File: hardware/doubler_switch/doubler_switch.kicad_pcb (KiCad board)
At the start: 2 copper layers, 54 parts, among them J101 CONN_01X06, U101 CONN_SMA_2GND, U102 PE42521, U103 74HC04_FULL, U104 AMMP-6120, U105 PE42521, U106 PE42521, U107 MASW-008322-TR1000, U108 PE42521, U109 CONN_SMA_2GND, U110 CONN_SMA_2GND, U111 TPS255xx, U112 LTC1983

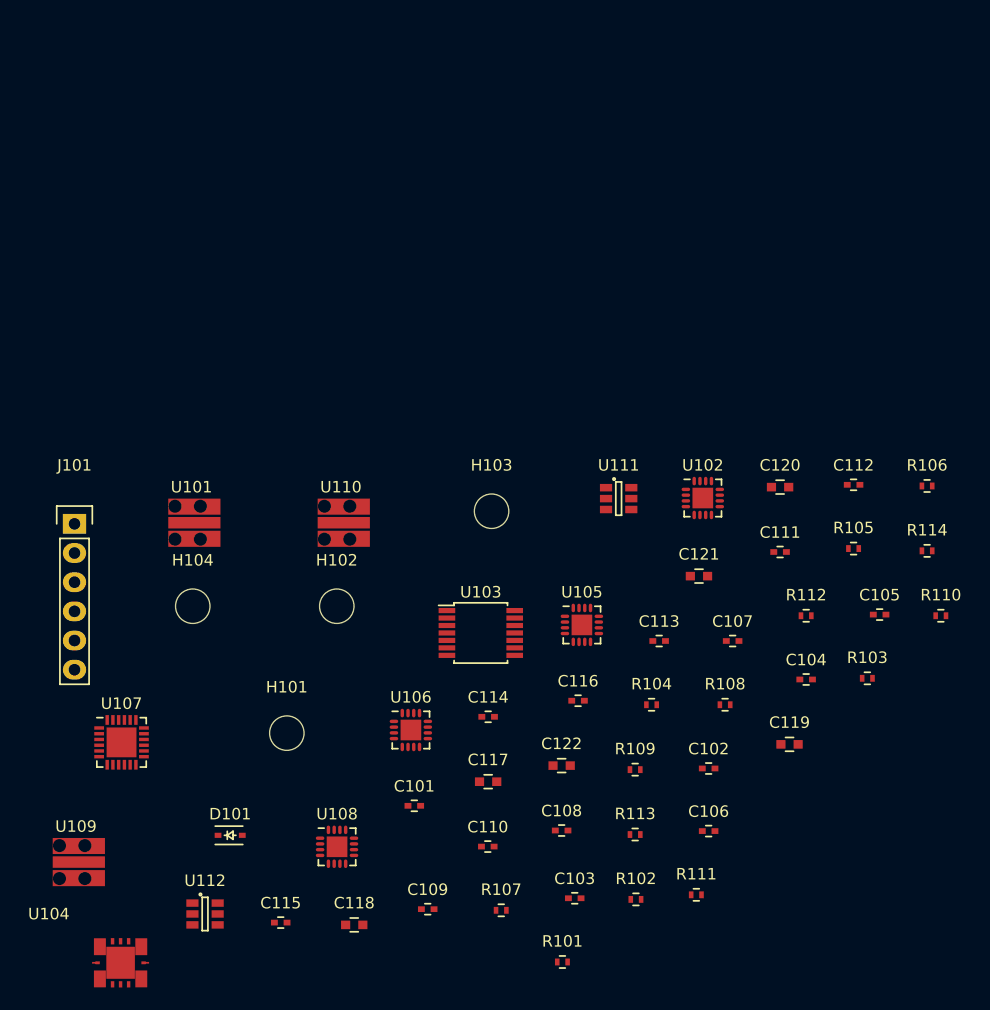
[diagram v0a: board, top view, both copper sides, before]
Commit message: finished vna port switch/multiplier board
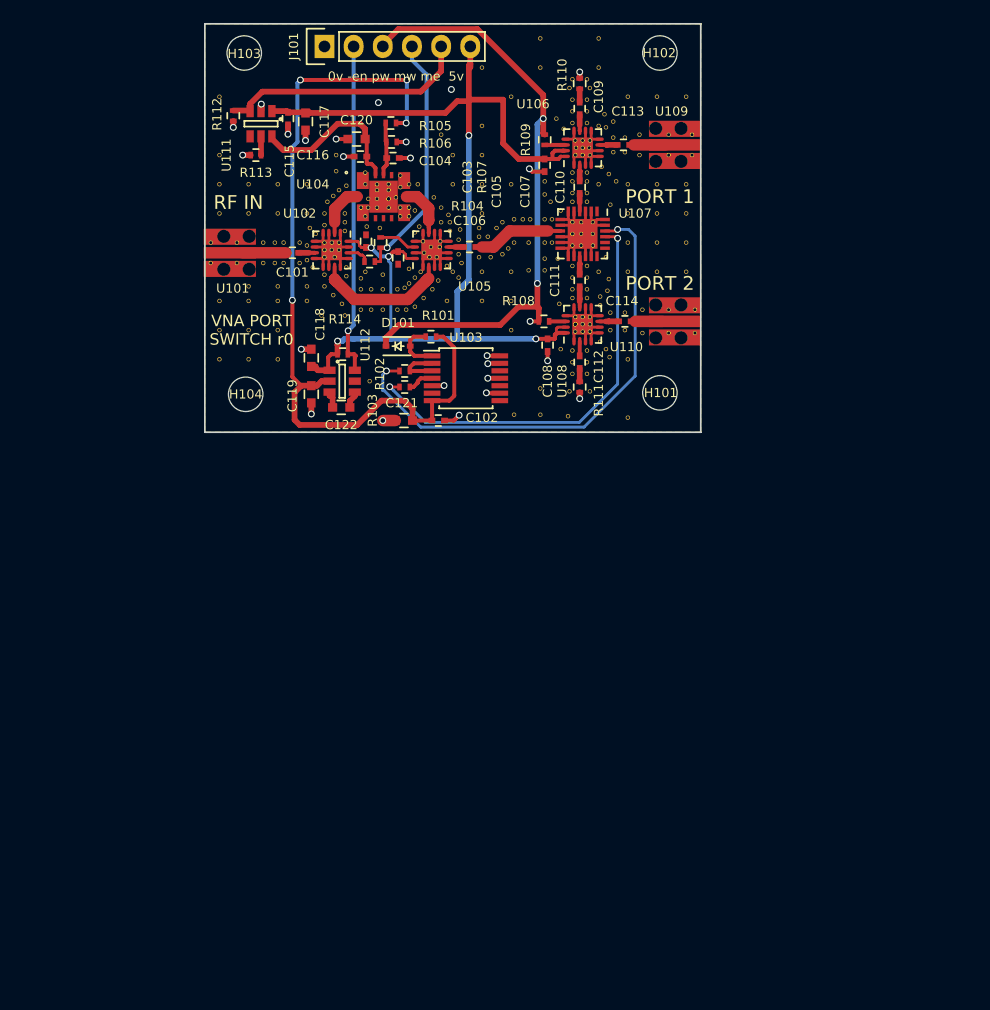
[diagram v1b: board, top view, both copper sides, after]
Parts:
- added REF**: VIA_OSH4LAYER_MIN, vna_footprints:VIA_OSH4LAYER_MIN, F.Cu at (229.7, 45.7)
- added REF**: VIA_OSH4LAYER_MIN, vna_footprints:VIA_OSH4LAYER_MIN, F.Cu at (218.2, 51.6)
- added REF**: VIA_OSH4LAYER_MIN, vna_footprints:VIA_OSH4LAYER_MIN, F.Cu at (238.8, 40.6)
- added REF**: VIA_OSH4LAYER_MIN, vna_footprints:VIA_OSH4LAYER_MIN, F.Cu at (238.8, 50.8)
- added REF**: VIA_OSH4LAYER_MIN, vna_footprints:VIA_OSH4LAYER_MIN, F.Cu at (233.7, 50.8)
- added REF**: VIA_OSH4LAYER_MIN, vna_footprints:VIA_OSH4LAYER_MIN, F.Cu at (238.8, 55.9)
- added REF**: VIA_OSH4LAYER_MIN, vna_footprints:VIA_OSH4LAYER_MIN, F.Cu at (238.8, 48.3)
- added REF**: VIA_OSH4LAYER_MIN, vna_footprints:VIA_OSH4LAYER_MIN, F.Cu at (238.8, 53.3)
- added REF**: VIA_OSH4LAYER_MIN, vna_footprints:VIA_OSH4LAYER_MIN, F.Cu at (233.7, 53.3)
- added REF**: VIA_OSH4LAYER_MIN, vna_footprints:VIA_OSH4LAYER_MIN, F.Cu at (236.2, 53.3)
- added REF**: VIA_OSH4LAYER_MIN, vna_footprints:VIA_OSH4LAYER_MIN, F.Cu at (223.5, 61.0)
- added REF**: VIA_OSH4LAYER_MIN, vna_footprints:VIA_OSH4LAYER_MIN, F.Cu at (226.4, 55.8)
- added REF**: VIA_OSH4LAYER_MIN, vna_footprints:VIA_OSH4LAYER_MIN, F.Cu at (218.9, 56.4)
- added REF**: VIA_OSH4LAYER_MIN, vna_footprints:VIA_OSH4LAYER_MIN, F.Cu at (231.1, 55.9)
- added REF**: VIA_OSH4LAYER_MIN, vna_footprints:VIA_OSH4LAYER_MIN, F.Cu at (233.7, 55.9)
- added REF**: VIA_OSH4LAYER_MIN, vna_footprints:VIA_OSH4LAYER_MIN, F.Cu at (236.2, 55.9)
- added REF**: VIA_OSH4LAYER_MIN, vna_footprints:VIA_OSH4LAYER_MIN, F.Cu at (236.2, 50.8)
- added REF**: VIA_OSH4LAYER_MIN, vna_footprints:VIA_OSH4LAYER_MIN, F.Cu at (236.2, 48.3)
- added REF**: VIA_OSH4LAYER_MIN, vna_footprints:VIA_OSH4LAYER_MIN, F.Cu at (233.7, 48.3)
- added REF**: VIA_OSH4LAYER_MIN, vna_footprints:VIA_OSH4LAYER_MIN, F.Cu at (231.1, 48.3)
- added REF**: VIA_OSH4LAYER_MIN, vna_footprints:VIA_OSH4LAYER_MIN, F.Cu at (231.1, 43.2)
- added REF**: VIA_OSH4LAYER_MIN, vna_footprints:VIA_OSH4LAYER_MIN, F.Cu at (221.0, 43.2)
- added REF**: VIA_OSH4LAYER_MIN, vna_footprints:VIA_OSH4LAYER_MIN, F.Cu at (221.0, 45.7)
- added REF**: VIA_OSH4LAYER_MIN, vna_footprints:VIA_OSH4LAYER_MIN, F.Cu at (217.9, 55.4)
- added REF**: VIA_OSH4LAYER_MIN, vna_footprints:VIA_OSH4LAYER_MIN, F.Cu at (226.4, 48.0)
- added REF**: VIA_OSH4LAYER_MIN, vna_footprints:VIA_OSH4LAYER_MIN, F.Cu at (223.5, 48.3)
- added REF**: VIA_OSH4LAYER_MIN, vna_footprints:VIA_OSH4LAYER_MIN, F.Cu at (221.0, 50.8)
- added REF**: VIA_OSH4LAYER_MIN, vna_footprints:VIA_OSH4LAYER_MIN, F.Cu at (221.0, 58.4)
- added REF**: VIA_OSH4LAYER_MIN, vna_footprints:VIA_OSH4LAYER_MIN, F.Cu at (217.9, 58.4)
- added REF**: VIA_OSH4LAYER_MIN, vna_footprints:VIA_OSH4LAYER_MIN, F.Cu at (223.5, 55.9)
- added REF**: VIA_OSH4LAYER_MIN, vna_footprints:VIA_OSH4LAYER_MIN, F.Cu at (221.0, 55.9)
- added REF**: VIA_OSH4LAYER_MIN, vna_footprints:VIA_OSH4LAYER_MIN, F.Cu at (218.4, 55.9)
- added REF**: VIA_OSH4LAYER_MIN, vna_footprints:VIA_OSH4LAYER_MIN, F.Cu at (218.4, 48.3)
- added REF**: VIA_OSH4LAYER_MIN, vna_footprints:VIA_OSH4LAYER_MIN, F.Cu at (208.3, 45.7)
- added REF**: VIA_OSH4LAYER_MIN, vna_footprints:VIA_OSH4LAYER_MIN, F.Cu at (227.7, 58.7)
- added REF**: VIA_OSH4LAYER_MIN, vna_footprints:VIA_OSH4LAYER_MIN, F.Cu at (205.7, 48.3)
- added REF**: VIA_OSH4LAYER_MIN, vna_footprints:VIA_OSH4LAYER_MIN, F.Cu at (203.2, 48.3)
- added REF**: VIA_OSH4LAYER_MIN, vna_footprints:VIA_OSH4LAYER_MIN, F.Cu at (200.7, 48.3)
- added REF**: VIA_OSH4LAYER_MIN, vna_footprints:VIA_OSH4LAYER_MIN, F.Cu at (198.1, 48.3)
- added REF**: VIA_OSH4LAYER_MIN, vna_footprints:VIA_OSH4LAYER_MIN, F.Cu at (198.1, 50.8)
- added REF**: VIA_OSH4LAYER_MIN, vna_footprints:VIA_OSH4LAYER_MIN, F.Cu at (200.7, 50.8)
- added REF**: VIA_OSH4LAYER_MIN, vna_footprints:VIA_OSH4LAYER_MIN, F.Cu at (203.2, 50.8)
- added REF**: VIA_OSH4LAYER_MIN, vna_footprints:VIA_OSH4LAYER_MIN, F.Cu at (203.2, 63.5)
- added REF**: VIA_OSH4LAYER_MIN, vna_footprints:VIA_OSH4LAYER_MIN, F.Cu at (198.1, 63.5)
- added REF**: VIA_OSH4LAYER_MIN, vna_footprints:VIA_OSH4LAYER_MIN, F.Cu at (198.1, 61.0)
- added REF**: VIA_OSH4LAYER_MIN, vna_footprints:VIA_OSH4LAYER_MIN, F.Cu at (227.8, 62.6)
- added REF**: VIA_OSH4LAYER_MIN, vna_footprints:VIA_OSH4LAYER_MIN, F.Cu at (203.2, 61.0)
- added REF**: VIA_OSH4LAYER_MIN, vna_footprints:VIA_OSH4LAYER_MIN, F.Cu at (200.7, 61.0)
- added REF**: VIA_OSH4LAYER_MIN, vna_footprints:VIA_OSH4LAYER_MIN, F.Cu at (200.7, 57.1)
- added REF**: VIA_OSH4LAYER_MIN, vna_footprints:VIA_OSH4LAYER_MIN, F.Cu at (203.2, 57.1)
- added REF**: VIA_OSH4LAYER_MIN, vna_footprints:VIA_OSH4LAYER_MIN, F.Cu at (205.7, 57.1)
- added REF**: VIA_OSH4LAYER_MIN, vna_footprints:VIA_OSH4LAYER_MIN, F.Cu at (209.0, 59.7)
- added REF**: VIA_OSH4LAYER_MIN, vna_footprints:VIA_OSH4LAYER_MIN, F.Cu at (230.1, 39.1)
- added REF**: VIA_OSH4LAYER_MIN, vna_footprints:VIA_OSH4LAYER_MIN, F.Cu at (228.9, 39.1)
- added REF**: VIA_OSH4LAYER_MIN, vna_footprints:VIA_OSH4LAYER_MIN, F.Cu at (228.6, 39.9)
- added REF**: VIA_OSH4LAYER_MIN, vna_footprints:VIA_OSH4LAYER_MIN, F.Cu at (230.4, 39.9)
- added REF**: VIA_OSH4LAYER_MIN, vna_footprints:VIA_OSH4LAYER_MIN, F.Cu at (232.0, 56.5)
- added REF**: VIA_OSH4LAYER_MIN, vna_footprints:VIA_OSH4LAYER_MIN, F.Cu at (230.1, 40.9)
- added REF**: VIA_OSH4LAYER_MIN, vna_footprints:VIA_OSH4LAYER_MIN, F.Cu at (228.9, 40.9)
- added REF**: VIA_OSH4LAYER_MIN, vna_footprints:VIA_OSH4LAYER_MIN, F.Cu at (228.9, 41.9)
- added REF**: VIA_OSH4LAYER_MIN, vna_footprints:VIA_OSH4LAYER_MIN, F.Cu at (230.1, 41.9)
- added REF**: VIA_OSH4LAYER_MIN, vna_footprints:VIA_OSH4LAYER_MIN, F.Cu at (230.1, 42.9)
- added REF**: VIA_OSH4LAYER_MIN, vna_footprints:VIA_OSH4LAYER_MIN, F.Cu at (228.9, 42.9)
- added REF**: VIA_OSH4LAYER_MIN, vna_footprints:VIA_OSH4LAYER_MIN, F.Cu at (228.6, 66.3)
- added REF**: VIA_OSH4LAYER_MIN, vna_footprints:VIA_OSH4LAYER_MIN, F.Cu at (230.4, 66.3)
- added REF**: VIA_OSH4LAYER_MIN, vna_footprints:VIA_OSH4LAYER_MIN, F.Cu at (230.1, 64.8)
- added REF**: VIA_OSH4LAYER_MIN, vna_footprints:VIA_OSH4LAYER_MIN, F.Cu at (228.9, 64.8)
- added REF**: VIA_OSH4LAYER_MIN, vna_footprints:VIA_OSH4LAYER_MIN, F.Cu at (231.9, 57.5)
- added REF**: VIA_OSH4LAYER_MIN, vna_footprints:VIA_OSH4LAYER_MIN, F.Cu at (228.9, 63.8)
- added REF**: VIA_OSH4LAYER_MIN, vna_footprints:VIA_OSH4LAYER_MIN, F.Cu at (230.1, 63.8)
- added REF**: VIA_OSH4LAYER_MIN, vna_footprints:VIA_OSH4LAYER_MIN, F.Cu at (230.1, 62.7)
- added REF**: VIA_OSH4LAYER_MIN, vna_footprints:VIA_OSH4LAYER_MIN, F.Cu at (228.9, 62.7)
- added REF**: VIA_OSH4LAYER_MIN, vna_footprints:VIA_OSH4LAYER_MIN, F.Cu at (228.9, 58.2)
- added REF**: VIA_OSH4LAYER_MIN, vna_footprints:VIA_OSH4LAYER_MIN, F.Cu at (230.1, 58.2)
- added REF**: VIA_OSH4LAYER_MIN, vna_footprints:VIA_OSH4LAYER_MIN, F.Cu at (230.1, 57.4)
- added REF**: VIA_OSH4LAYER_MIN, vna_footprints:VIA_OSH4LAYER_MIN, F.Cu at (228.9, 57.4)
- added REF**: VIA_OSH4LAYER_MIN, vna_footprints:VIA_OSH4LAYER_MIN, F.Cu at (228.9, 56.4)
- added REF**: VIA_OSH4LAYER_MIN, vna_footprints:VIA_OSH4LAYER_MIN, F.Cu at (230.1, 56.4)
- added REF**: VIA_OSH4LAYER_MIN, vna_footprints:VIA_OSH4LAYER_MIN, F.Cu at (231.3, 58.0)
- added REF**: VIA_OSH4LAYER_MIN, vna_footprints:VIA_OSH4LAYER_MIN, F.Cu at (230.1, 55.4)
- added REF**: VIA_OSH4LAYER_MIN, vna_footprints:VIA_OSH4LAYER_MIN, F.Cu at (228.9, 55.4)
- added REF**: VIA_OSH4LAYER_MIN, vna_footprints:VIA_OSH4LAYER_MIN, F.Cu at (228.9, 47.2)
- added REF**: VIA_OSH4LAYER_MIN, vna_footprints:VIA_OSH4LAYER_MIN, F.Cu at (230.1, 47.2)
- added REF**: VIA_OSH4LAYER_MIN, vna_footprints:VIA_OSH4LAYER_MIN, F.Cu at (230.1, 48.0)
- added REF**: VIA_OSH4LAYER_MIN, vna_footprints:VIA_OSH4LAYER_MIN, F.Cu at (228.9, 48.0)
- added REF**: VIA_OSH4LAYER_MIN, vna_footprints:VIA_OSH4LAYER_MIN, F.Cu at (228.9, 49.0)
- added REF**: VIA_OSH4LAYER_MIN, vna_footprints:VIA_OSH4LAYER_MIN, F.Cu at (230.1, 49.0)
- added REF**: VIA_OSH4LAYER_MIN, vna_footprints:VIA_OSH4LAYER_MIN, F.Cu at (230.1, 49.8)
- added REF**: VIA_OSH4LAYER_MIN, vna_footprints:VIA_OSH4LAYER_MIN, F.Cu at (228.9, 49.8)
- added REF**: VIA_OSH4LAYER_MIN, vna_footprints:VIA_OSH4LAYER_MIN, F.Cu at (231.3, 58.8)
- added REF**: VIA_OSH4LAYER_MIN, vna_footprints:VIA_OSH4LAYER_MIN, F.Cu at (227.1, 53.3)
- added REF**: VIA_OSH4LAYER_MIN, vna_footprints:VIA_OSH4LAYER_MIN, F.Cu at (227.1, 51.3)
- added REF**: VIA_OSH4LAYER_MIN, vna_footprints:VIA_OSH4LAYER_MIN, F.Cu at (226.4, 53.3)
- added REF**: VIA_OSH4LAYER_MIN, vna_footprints:VIA_OSH4LAYER_MIN, F.Cu at (226.4, 51.3)
- added REF**: VIA_OSH4LAYER_MIN, vna_footprints:VIA_OSH4LAYER_MIN, F.Cu at (225.2, 51.3)
- added REF**: VIA_OSH4LAYER_MIN, vna_footprints:VIA_OSH4LAYER_MIN, F.Cu at (225.0, 53.3)
- added REF**: VIA_OSH4LAYER_MIN, vna_footprints:VIA_OSH4LAYER_MIN, F.Cu at (224.5, 51.3)
- added REF**: VIA_OSH4LAYER_MIN, vna_footprints:VIA_OSH4LAYER_MIN, F.Cu at (223.8, 51.3)
- added REF**: VIA_OSH4LAYER_MIN, vna_footprints:VIA_OSH4LAYER_MIN, F.Cu at (222.8, 51.6)
- added REF**: VIA_OSH4LAYER_MIN, vna_footprints:VIA_OSH4LAYER_MIN, F.Cu at (223.8, 53.3)
- added REF**: VIA_OSH4LAYER_MIN, vna_footprints:VIA_OSH4LAYER_MIN, F.Cu at (232.1, 63.3)
- added REF**: VIA_OSH4LAYER_MIN, vna_footprints:VIA_OSH4LAYER_MIN, F.Cu at (223.3, 53.8)
- added REF**: VIA_OSH4LAYER_MIN, vna_footprints:VIA_OSH4LAYER_MIN, F.Cu at (222.8, 54.4)
- added REF**: VIA_OSH4LAYER_MIN, vna_footprints:VIA_OSH4LAYER_MIN, F.Cu at (222.2, 52.1)
- added REF**: VIA_OSH4LAYER_MIN, vna_footprints:VIA_OSH4LAYER_MIN, F.Cu at (221.5, 52.8)
- added REF**: VIA_OSH4LAYER_MIN, vna_footprints:VIA_OSH4LAYER_MIN, F.Cu at (221.7, 54.6)
- added REF**: VIA_OSH4LAYER_MIN, vna_footprints:VIA_OSH4LAYER_MIN, F.Cu at (220.7, 52.8)
- added REF**: VIA_OSH4LAYER_MIN, vna_footprints:VIA_OSH4LAYER_MIN, F.Cu at (220.7, 54.6)
- added REF**: VIA_OSH4LAYER_MIN, vna_footprints:VIA_OSH4LAYER_MIN, F.Cu at (220.7, 52.1)
- added REF**: VIA_OSH4LAYER_MIN, vna_footprints:VIA_OSH4LAYER_MIN, F.Cu at (218.9, 53.1)
- added REF**: VIA_OSH4LAYER_MIN, vna_footprints:VIA_OSH4LAYER_MIN, F.Cu at (218.9, 54.4)
- added REF**: VIA_OSH4LAYER_MIN, vna_footprints:VIA_OSH4LAYER_MIN, F.Cu at (229.7, 44.5)
- added REF**: VIA_OSH4LAYER_MIN, vna_footprints:VIA_OSH4LAYER_MIN, F.Cu at (231.8, 62.6)
- added REF**: VIA_OSH4LAYER_MIN, vna_footprints:VIA_OSH4LAYER_MIN, F.Cu at (209.2, 55.5)
- added REF**: VIA_OSH4LAYER_MIN, vna_footprints:VIA_OSH4LAYER_MIN, F.Cu at (209.2, 56.3)
- added REF**: VIA_OSH4LAYER_MIN, vna_footprints:VIA_OSH4LAYER_MIN, F.Cu at (210.4, 56.5)
- added REF**: VIA_OSH4LAYER_MIN, vna_footprints:VIA_OSH4LAYER_MIN, F.Cu at (210.4, 57.4)
- added REF**: VIA_OSH4LAYER_MIN, vna_footprints:VIA_OSH4LAYER_MIN, F.Cu at (211.3, 57.4)
- added REF**: VIA_OSH4LAYER_MIN, vna_footprints:VIA_OSH4LAYER_MIN, F.Cu at (212.3, 57.4)
- added REF**: VIA_OSH4LAYER_MIN, vna_footprints:VIA_OSH4LAYER_MIN, F.Cu at (213.6, 57.4)
- added REF**: VIA_OSH4LAYER_MIN, vna_footprints:VIA_OSH4LAYER_MIN, F.Cu at (214.2, 57.3)
- added REF**: VIA_OSH4LAYER_MIN, vna_footprints:VIA_OSH4LAYER_MIN, F.Cu at (214.6, 56.9)
- added REF**: VIA_OSH4LAYER_MIN, vna_footprints:VIA_OSH4LAYER_MIN, F.Cu at (215.1, 56.4)
- added REF**: VIA_OSH4LAYER_MIN, vna_footprints:VIA_OSH4LAYER_MIN, F.Cu at (231.3, 62.0)
- added REF**: VIA_OSH4LAYER_MIN, vna_footprints:VIA_OSH4LAYER_MIN, F.Cu at (215.6, 55.9)
- added REF**: VIA_OSH4LAYER_MIN, vna_footprints:VIA_OSH4LAYER_MIN, F.Cu at (217.2, 56.6)
- added REF**: VIA_OSH4LAYER_MIN, vna_footprints:VIA_OSH4LAYER_MIN, F.Cu at (216.7, 57.4)
- added REF**: VIA_OSH4LAYER_MIN, vna_footprints:VIA_OSH4LAYER_MIN, F.Cu at (215.9, 58.2)
- added REF**: VIA_OSH4LAYER_MIN, vna_footprints:VIA_OSH4LAYER_MIN, F.Cu at (215.1, 58.9)
- added REF**: VIA_OSH4LAYER_MIN, vna_footprints:VIA_OSH4LAYER_MIN, F.Cu at (214.4, 59.2)
- added REF**: VIA_OSH4LAYER_MIN, vna_footprints:VIA_OSH4LAYER_MIN, F.Cu at (213.6, 59.2)
- added REF**: VIA_OSH4LAYER_MIN, vna_footprints:VIA_OSH4LAYER_MIN, F.Cu at (212.3, 59.2)
- added REF**: VIA_OSH4LAYER_MIN, vna_footprints:VIA_OSH4LAYER_MIN, F.Cu at (211.3, 59.2)
- added REF**: VIA_OSH4LAYER_MIN, vna_footprints:VIA_OSH4LAYER_MIN, F.Cu at (210.4, 59.2)
- added REF**: VIA_OSH4LAYER_MIN, vna_footprints:VIA_OSH4LAYER_MIN, F.Cu at (230.4, 61.1)
- added REF**: VIA_OSH4LAYER_MIN, vna_footprints:VIA_OSH4LAYER_MIN, F.Cu at (208.8, 58.7)
- added REF**: VIA_OSH4LAYER_MIN, vna_footprints:VIA_OSH4LAYER_MIN, F.Cu at (208.0, 57.9)
- added REF**: VIA_OSH4LAYER_MIN, vna_footprints:VIA_OSH4LAYER_MIN, F.Cu at (207.3, 57.1)
- added REF**: VIA_OSH4LAYER_MIN, vna_footprints:VIA_OSH4LAYER_MIN, F.Cu at (207.3, 56.1)
- added REF**: VIA_OSH4LAYER_MIN, vna_footprints:VIA_OSH4LAYER_MIN, F.Cu at (209.2, 48.4)
- added REF**: VIA_OSH4LAYER_MIN, vna_footprints:VIA_OSH4LAYER_MIN, F.Cu at (208.5, 48.8)
- added REF**: VIA_OSH4LAYER_MIN, vna_footprints:VIA_OSH4LAYER_MIN, F.Cu at (208.0, 49.3)
- added REF**: VIA_OSH4LAYER_MIN, vna_footprints:VIA_OSH4LAYER_MIN, F.Cu at (207.5, 49.8)
- added REF**: VIA_OSH4LAYER_MIN, vna_footprints:VIA_OSH4LAYER_MIN, F.Cu at (207.3, 50.8)
- added REF**: VIA_OSH4LAYER_MIN, vna_footprints:VIA_OSH4LAYER_MIN, F.Cu at (207.3, 51.8)
- added REF**: VIA_OSH4LAYER_MIN, vna_footprints:VIA_OSH4LAYER_MIN, F.Cu at (229.7, 61.1)
- added REF**: VIA_OSH4LAYER_MIN, vna_footprints:VIA_OSH4LAYER_MIN, F.Cu at (209.0, 52.3)
- added REF**: VIA_OSH4LAYER_MIN, vna_footprints:VIA_OSH4LAYER_MIN, F.Cu at (209.0, 51.6)
- added REF**: VIA_OSH4LAYER_MIN, vna_footprints:VIA_OSH4LAYER_MIN, F.Cu at (209.0, 50.8)
- added REF**: VIA_OSH4LAYER_MIN, vna_footprints:VIA_OSH4LAYER_MIN, F.Cu at (215.5, 51.9)
- added REF**: VIA_OSH4LAYER_MIN, vna_footprints:VIA_OSH4LAYER_MIN, F.Cu at (217.4, 51.6)
- added REF**: VIA_OSH4LAYER_MIN, vna_footprints:VIA_OSH4LAYER_MIN, F.Cu at (217.4, 50.3)
- added REF**: VIA_OSH4LAYER_MIN, vna_footprints:VIA_OSH4LAYER_MIN, F.Cu at (216.8, 49.4)
- added REF**: VIA_OSH4LAYER_MIN, vna_footprints:VIA_OSH4LAYER_MIN, F.Cu at (215.1, 50.5)
- added REF**: VIA_OSH4LAYER_MIN, vna_footprints:VIA_OSH4LAYER_MIN, F.Cu at (215.4, 48.3)
- added REF**: VIA_OSH4LAYER_MIN, vna_footprints:VIA_OSH4LAYER_MIN, F.Cu at (214.6, 48.3)
- added REF**: VIA_OSH4LAYER_MIN, vna_footprints:VIA_OSH4LAYER_MIN, F.Cu at (229.1, 61.1)
- added REF**: VIA_OSH4LAYER_MIN, vna_footprints:VIA_OSH4LAYER_MIN, F.Cu at (210.8, 47.2)
- added REF**: VIA_OSH4LAYER_MIN, vna_footprints:VIA_OSH4LAYER_MIN, F.Cu at (208.3, 47.1)
- added REF**: VIA_OSH4LAYER_MIN, vna_footprints:VIA_OSH4LAYER_MIN, F.Cu at (212.1, 52.1)
- added REF**: VIA_OSH4LAYER_MIN, vna_footprints:VIA_OSH4LAYER_MIN, F.Cu at (210.8, 51.1)
- added REF**: VIA_OSH4LAYER_MIN, vna_footprints:VIA_OSH4LAYER_MIN, F.Cu at (213.9, 51.1)
- added REF**: VIA_OSH4LAYER_MIN, vna_footprints:VIA_OSH4LAYER_MIN, F.Cu at (214.6, 51.1)
- added REF**: VIA_OSH4LAYER_MIN, vna_footprints:VIA_OSH4LAYER_MIN, F.Cu at (214.6, 50.3)
- added REF**: VIA_OSH4LAYER_MIN, vna_footprints:VIA_OSH4LAYER_MIN, F.Cu at (211.8, 48.3)
- added REF**: VIA_OSH4LAYER_MIN, vna_footprints:VIA_OSH4LAYER_MIN, F.Cu at (212.9, 48.3)
- added REF**: VIA_OSH4LAYER_MIN, vna_footprints:VIA_OSH4LAYER_MIN, F.Cu at (213.9, 47.5)
- added REF** (x2): VIA_OSH4LAYER_MIN, vna_footprints:VIA_OSH4LAYER_MIN, F.Cu at (229.1, 60.5)
- added REF**: VIA_OSH4LAYER_MIN, vna_footprints:VIA_OSH4LAYER_MIN, F.Cu at (213.9, 48.5)
- added REF**: VIA_OSH4LAYER_MIN, vna_footprints:VIA_OSH4LAYER_MIN, F.Cu at (212.9, 48.8)
- added REF**: VIA_OSH4LAYER_MIN, vna_footprints:VIA_OSH4LAYER_MIN, F.Cu at (211.8, 48.8)
- added REF**: VIA_OSH4LAYER_MIN, vna_footprints:VIA_OSH4LAYER_MIN, F.Cu at (211.1, 49.5)
- added REF**: VIA_OSH4LAYER_MIN, vna_footprints:VIA_OSH4LAYER_MIN, F.Cu at (211.8, 49.5)
- added REF** (x2): VIA_OSH4LAYER_MIN, vna_footprints:VIA_OSH4LAYER_MIN, F.Cu at (212.9, 49.5)
- added REF**: VIA_OSH4LAYER_MIN, vna_footprints:VIA_OSH4LAYER_MIN, F.Cu at (213.9, 50.3)
- added REF**: VIA_OSH4LAYER_MIN, vna_footprints:VIA_OSH4LAYER_MIN, F.Cu at (212.9, 50.3)
- added REF**: VIA_OSH4LAYER_MIN, vna_footprints:VIA_OSH4LAYER_MIN, F.Cu at (211.8, 50.3)
- added REF**: VIA_OSH4LAYER_MIN, vna_footprints:VIA_OSH4LAYER_MIN, F.Cu at (211.1, 50.3)
- added REF**: VIA_OSH4LAYER_MIN, vna_footprints:VIA_OSH4LAYER_MIN, F.Cu at (210.8, 48.3)
- added REF**: VIA_OSH4LAYER_MIN, vna_footprints:VIA_OSH4LAYER_MIN, F.Cu at (213.5, 49.4)
- added REF**: VIA_OSH4LAYER_MIN, vna_footprints:VIA_OSH4LAYER_MIN, F.Cu at (230.6, 53.6)
- added REF**: VIA_OSH4LAYER_MIN, vna_footprints:VIA_OSH4LAYER_MIN, F.Cu at (229.6, 53.6)
- added REF**: VIA_OSH4LAYER_MIN, vna_footprints:VIA_OSH4LAYER_MIN, F.Cu at (228.9, 53.6)
- added REF**: VIA_OSH4LAYER_MIN, vna_footprints:VIA_OSH4LAYER_MIN, F.Cu at (228.9, 52.6)
- added REF**: VIA_OSH4LAYER_MIN, vna_footprints:VIA_OSH4LAYER_MIN, F.Cu at (229.6, 52.6)
- added REF**: VIA_OSH4LAYER_MIN, vna_footprints:VIA_OSH4LAYER_MIN, F.Cu at (230.6, 52.6)
- added REF**: VIA_OSH4LAYER_MIN, vna_footprints:VIA_OSH4LAYER_MIN, F.Cu at (230.6, 51.6)
- added REF**: VIA_OSH4LAYER_MIN, vna_footprints:VIA_OSH4LAYER_MIN, F.Cu at (229.7, 60.5)
- added REF**: VIA_OSH4LAYER_MIN, vna_footprints:VIA_OSH4LAYER_MIN, F.Cu at (229.6, 51.6)
- added REF**: VIA_OSH4LAYER_MIN, vna_footprints:VIA_OSH4LAYER_MIN, F.Cu at (228.9, 51.6)
- added REF**: VIA_OSH4LAYER_MIN, vna_footprints:VIA_OSH4LAYER_MIN, F.Cu at (230.4, 45.7)
- added REF**: VIA_OSH4LAYER_MIN, vna_footprints:VIA_OSH4LAYER_MIN, F.Cu at (229.1, 45.7)
- added REF**: VIA_OSH4LAYER_MIN, vna_footprints:VIA_OSH4LAYER_MIN, F.Cu at (229.1, 44.5)
- added REF**: VIA_OSH4LAYER_MIN, vna_footprints:VIA_OSH4LAYER_MIN, F.Cu at (230.4, 44.5)
- added REF**: VIA_OSH4LAYER_MIN, vna_footprints:VIA_OSH4LAYER_MIN, F.Cu at (232.4, 44.2)
- added REF**: VIA_OSH4LAYER_MIN, vna_footprints:VIA_OSH4LAYER_MIN, F.Cu at (232.4, 45.5)
- added REF**: VIA_OSH4LAYER_MIN, vna_footprints:VIA_OSH4LAYER_MIN, F.Cu at (233.4, 45.5)
- added REF**: VIA_OSH4LAYER_MIN, vna_footprints:VIA_OSH4LAYER_MIN, F.Cu at (233.4, 44.2)
- added REF**: VIA_OSH4LAYER_MIN, vna_footprints:VIA_OSH4LAYER_MIN, F.Cu at (230.4, 60.5)
- added REF**: VIA_OSH4LAYER_MIN, vna_footprints:VIA_OSH4LAYER_MIN, F.Cu at (234.7, 43.9)
- added REF**: VIA_OSH4LAYER_MIN, vna_footprints:VIA_OSH4LAYER_MIN, F.Cu at (234.7, 45.7)
- added REF**: VIA_OSH4LAYER_MIN, vna_footprints:VIA_OSH4LAYER_MIN, F.Cu at (239.3, 45.7)
- added REF**: VIA_OSH4LAYER_MIN, vna_footprints:VIA_OSH4LAYER_MIN, F.Cu at (239.3, 43.9)
- added REF**: VIA_OSH4LAYER_MIN, vna_footprints:VIA_OSH4LAYER_MIN, F.Cu at (237.2, 43.9)
- added REF**: VIA_OSH4LAYER_MIN, vna_footprints:VIA_OSH4LAYER_MIN, F.Cu at (237.2, 45.7)
- added REF**: VIA_OSH4LAYER_MIN, vna_footprints:VIA_OSH4LAYER_MIN, F.Cu at (232.2, 61.0)
- added REF**: VIA_OSH4LAYER_MIN, vna_footprints:VIA_OSH4LAYER_MIN, F.Cu at (232.2, 59.4)
- added REF**: VIA_OSH4LAYER_MIN, vna_footprints:VIA_OSH4LAYER_MIN, F.Cu at (233.4, 59.4)
- added REF**: VIA_OSH4LAYER_MIN, vna_footprints:VIA_OSH4LAYER_MIN, F.Cu at (233.4, 61.0)
- added REF**: VIA_OSH4LAYER_MIN, vna_footprints:VIA_OSH4LAYER_MIN, F.Cu at (230.4, 59.8)
- added REF**: VIA_OSH4LAYER_MIN, vna_footprints:VIA_OSH4LAYER_MIN, F.Cu at (234.9, 61.2)
- added REF**: VIA_OSH4LAYER_MIN, vna_footprints:VIA_OSH4LAYER_MIN, F.Cu at (234.9, 59.2)
- added REF**: VIA_OSH4LAYER_MIN, vna_footprints:VIA_OSH4LAYER_MIN, F.Cu at (239.5, 59.2)
- added REF**: VIA_OSH4LAYER_MIN, vna_footprints:VIA_OSH4LAYER_MIN, F.Cu at (237.2, 59.2)
- added REF**: VIA_OSH4LAYER_MIN, vna_footprints:VIA_OSH4LAYER_MIN, F.Cu at (237.2, 61.2)
- added REF**: VIA_OSH4LAYER_MIN, vna_footprints:VIA_OSH4LAYER_MIN, F.Cu at (239.5, 61.2)
- added REF**: VIA_OSH4LAYER_MIN, vna_footprints:VIA_OSH4LAYER_MIN, F.Cu at (203.7, 55.1)
- added REF**: VIA_OSH4LAYER_MIN, vna_footprints:VIA_OSH4LAYER_MIN, F.Cu at (203.7, 53.3)
- added REF**: VIA_OSH4LAYER_MIN, vna_footprints:VIA_OSH4LAYER_MIN, F.Cu at (205.7, 53.6)
- added REF**: VIA_OSH4LAYER_MIN, vna_footprints:VIA_OSH4LAYER_MIN, F.Cu at (205.7, 54.9)
- added REF**: VIA_OSH4LAYER_MIN, vna_footprints:VIA_OSH4LAYER_MIN, F.Cu at (230.3, 45.1)
- added REF**: VIA_OSH4LAYER_MIN, vna_footprints:VIA_OSH4LAYER_MIN, F.Cu at (229.7, 59.8)
- added REF**: VIA_OSH4LAYER_MIN, vna_footprints:VIA_OSH4LAYER_MIN, F.Cu at (205.1, 55.1)
- added REF**: VIA_OSH4LAYER_MIN, vna_footprints:VIA_OSH4LAYER_MIN, F.Cu at (205.1, 53.3)
- added REF**: VIA_OSH4LAYER_MIN, vna_footprints:VIA_OSH4LAYER_MIN, F.Cu at (202.9, 53.3)
- added REF**: VIA_OSH4LAYER_MIN, vna_footprints:VIA_OSH4LAYER_MIN, F.Cu at (202.9, 55.1)
- added REF**: VIA_OSH4LAYER_MIN, vna_footprints:VIA_OSH4LAYER_MIN, F.Cu at (201.9, 55.1)
- added REF**: VIA_OSH4LAYER_MIN, vna_footprints:VIA_OSH4LAYER_MIN, F.Cu at (199.6, 55.1)
- added REF**: VIA_OSH4LAYER_MIN, vna_footprints:VIA_OSH4LAYER_MIN, F.Cu at (197.4, 55.1)
- added REF**: VIA_OSH4LAYER_MIN, vna_footprints:VIA_OSH4LAYER_MIN, F.Cu at (197.4, 53.3)
- added REF**: VIA_OSH4LAYER_MIN, vna_footprints:VIA_OSH4LAYER_MIN, F.Cu at (199.6, 53.3)
- added REF**: VIA_OSH4LAYER_MIN, vna_footprints:VIA_OSH4LAYER_MIN, F.Cu at (201.9, 53.3)
- added REF**: VIA_OSH4LAYER_MIN, vna_footprints:VIA_OSH4LAYER_MIN, F.Cu at (229.1, 59.8)
- added REF**: VIA_OSH4LAYER_MIN, vna_footprints:VIA_OSH4LAYER_MIN, F.Cu at (228.1, 43.4)
- added REF**: VIA_OSH4LAYER_MIN, vna_footprints:VIA_OSH4LAYER_MIN, F.Cu at (232.4, 42.8)
- added REF**: VIA_OSH4LAYER_MIN, vna_footprints:VIA_OSH4LAYER_MIN, F.Cu at (231.8, 43.3)
- added REF**: VIA_OSH4LAYER_MIN, vna_footprints:VIA_OSH4LAYER_MIN, F.Cu at (232.7, 48.0)
- added REF**: VIA_OSH4LAYER_MIN, vna_footprints:VIA_OSH4LAYER_MIN, F.Cu at (232.0, 47.4)
- added REF**: VIA_OSH4LAYER_MIN, vna_footprints:VIA_OSH4LAYER_MIN, F.Cu at (231.4, 46.7)
- added REF**: VIA_OSH4LAYER_MIN, vna_footprints:VIA_OSH4LAYER_MIN, F.Cu at (232.2, 50.0)
- added REF**: VIA_OSH4LAYER_MIN, vna_footprints:VIA_OSH4LAYER_MIN, F.Cu at (231.8, 54.6)
- added REF**: VIA_OSH4LAYER_MIN, vna_footprints:VIA_OSH4LAYER_MIN, F.Cu at (229.2, 45.1)
- added REF**: VIA_OSH4LAYER_MIN, vna_footprints:VIA_OSH4LAYER_MIN, F.Cu at (225.0, 55.8)
- added REF**: VIA_OSH4LAYER_MIN, vna_footprints:VIA_OSH4LAYER_MIN, F.Cu at (226.4, 54.7)
- added REF**: VIA_OSH4LAYER_MIN, vna_footprints:VIA_OSH4LAYER_MIN, F.Cu at (227.6, 54.7)
- added REF**: VIA_OSH4LAYER_MIN, vna_footprints:VIA_OSH4LAYER_MIN, F.Cu at (226.4, 49.1)
- added REF**: VIA_OSH4LAYER_MIN, vna_footprints:VIA_OSH4LAYER_MIN, F.Cu at (226.9, 49.8)
- added REF**: VIA_OSH4LAYER_MIN, vna_footprints:VIA_OSH4LAYER_MIN, F.Cu at (227.8, 50.5)
- added REF**: VIA_OSH4LAYER_MIN, vna_footprints:VIA_OSH4LAYER_MIN, F.Cu at (219.2, 55.1)
- added REF**: VIA_OSH4LAYER_MIN, vna_footprints:VIA_OSH4LAYER_MIN, F.Cu at (218.1, 50.9)
- added REF**: VIA_OSH4LAYER_MIN, vna_footprints:VIA_OSH4LAYER_MIN, F.Cu at (219.1, 52.2)
- added REF**: VIA_OSH4LAYER_MIN, vna_footprints:VIA_OSH4LAYER_MIN, F.Cu at (216.5, 53.7)
- added REF**: VIA_OSH4LAYER_MIN, vna_footprints:VIA_OSH4LAYER_MIN, F.Cu at (229.7, 45.1)
- added REF**: VIA_OSH4LAYER_MIN, vna_footprints:VIA_OSH4LAYER_MIN, F.Cu at (214.6, 55.6)
- added REF**: VIA_OSH4LAYER_MIN, vna_footprints:VIA_OSH4LAYER_MIN, F.Cu at (218.2, 52.3)
- added REF**: VIA_OSH4LAYER_MIN, vna_footprints:VIA_OSH4LAYER_MIN, F.Cu at (215.1, 52.5)
- added REF**: VIA_OSH4LAYER_MIN, vna_footprints:VIA_OSH4LAYER_MIN, F.Cu at (217.0, 54.6)
- added REF**: VIA_OSH4LAYER_MIN, vna_footprints:VIA_OSH4LAYER_MIN, F.Cu at (217.3, 53.7)
- added REF**: VIA_OSH4LAYER_MIN, vna_footprints:VIA_OSH4LAYER_MIN, F.Cu at (216.4, 54.6)
- added REF**: VIA_OSH4LAYER_MIN, vna_footprints:VIA_OSH4LAYER_MIN, F.Cu at (215.9, 54.2)
- added REF**: VIA_OSH4LAYER_MIN, vna_footprints:VIA_OSH4LAYER_MIN, F.Cu at (215.8, 53.2)
- added REF**: VIA_OSH4LAYER_MIN, vna_footprints:VIA_OSH4LAYER_MIN, F.Cu at (217.3, 53.2)
- added REF**: VIA_OSH4LAYER_MIN, vna_footprints:VIA_OSH4LAYER_MIN, F.Cu at (210.9, 51.9)
- added REF**: VIA_OSH4LAYER_MIN, vna_footprints:VIA_OSH4LAYER_MIN, F.Cu at (207.0, 59.7)
- added REF**: VIA_OSH4LAYER_MIN, vna_footprints:VIA_OSH4LAYER_MIN, F.Cu at (206.2, 55.5)
- added REF**: VIA_OSH4LAYER_MIN, vna_footprints:VIA_OSH4LAYER_MIN, F.Cu at (206.0, 52.1)
- added REF**: VIA_OSH4LAYER_MIN, vna_footprints:VIA_OSH4LAYER_MIN, F.Cu at (206.5, 52.6)
- added REF**: VIA_OSH4LAYER_MIN, vna_footprints:VIA_OSH4LAYER_MIN, F.Cu at (208.5, 54.0)
- added REF**: VIA_OSH4LAYER_MIN, vna_footprints:VIA_OSH4LAYER_MIN, F.Cu at (208.5, 53.3)
- added REF**: VIA_OSH4LAYER_MIN, vna_footprints:VIA_OSH4LAYER_MIN, F.Cu at (208.2, 54.6)
- added REF**: VIA_OSH4LAYER_MIN, vna_footprints:VIA_OSH4LAYER_MIN, F.Cu at (207.9, 54.0)
- added REF**: VIA_OSH4LAYER_MIN, vna_footprints:VIA_OSH4LAYER_MIN, F.Cu at (207.9, 53.3)
- added REF**: VIA_OSH4LAYER_MIN, vna_footprints:VIA_OSH4LAYER_MIN, F.Cu at (207.3, 53.3)
- added REF**: VIA_OSH4LAYER_MIN, vna_footprints:VIA_OSH4LAYER_MIN, F.Cu at (207.3, 54.0)
- added REF**: VIA_OSH4LAYER_MIN, vna_footprints:VIA_OSH4LAYER_MIN, F.Cu at (211.2, 65.4)
- added REF**: VIA_OSH4LAYER_MIN, vna_footprints:VIA_OSH4LAYER_MIN, F.Cu at (207.3, 54.6)
- added REF**: VIA_OSH4LAYER_MIN, vna_footprints:VIA_OSH4LAYER_MIN, F.Cu at (210.4, 50.3)
- added REF**: VIA_OSH4LAYER_MIN, vna_footprints:VIA_OSH4LAYER_MIN, F.Cu at (217.4, 43.9)
- added REF**: VIA_OSH4LAYER_MIN, vna_footprints:VIA_OSH4LAYER_MIN, F.Cu at (221.0, 38.1)
- added REF**: VIA_OSH4LAYER_MIN, vna_footprints:VIA_OSH4LAYER_MIN, F.Cu at (205.7, 58.4)
- added REF**: VIA_OSH4LAYER_MIN, vna_footprints:VIA_OSH4LAYER_MIN, F.Cu at (210.8, 55.9)
- added REF**: VIA_OSH4LAYER_MIN, vna_footprints:VIA_OSH4LAYER_MIN, F.Cu at (212.3, 56.1)
- added REF**: VIA_OSH4LAYER_MIN, vna_footprints:VIA_OSH4LAYER_MIN, F.Cu at (226.1, 38.1)
- added REF**: VIA_OSH4LAYER_MIN, vna_footprints:VIA_OSH4LAYER_MIN, F.Cu at (221.0, 48.3)
- added REF**: VIA_OSH4LAYER_MIN, vna_footprints:VIA_OSH4LAYER_MIN, F.Cu at (198.1, 40.6)
- added REF**: VIA_OSH4LAYER_MIN, vna_footprints:VIA_OSH4LAYER_MIN, F.Cu at (231.6, 42.2)
- added REF**: VIA_OSH4LAYER_MIN, vna_footprints:VIA_OSH4LAYER_MIN, F.Cu at (198.1, 45.7)
- added REF**: VIA_OSH4LAYER_MIN, vna_footprints:VIA_OSH4LAYER_MIN, F.Cu at (223.5, 58.4)
- added REF**: VIA_OSH4LAYER_MIN, vna_footprints:VIA_OSH4LAYER_MIN, F.Cu at (226.1, 66.0)
- added REF**: VIA_OSH4LAYER_MIN, vna_footprints:VIA_OSH4LAYER_MIN, F.Cu at (233.7, 68.6)
- added REF**: VIA_OSH4LAYER_MIN, vna_footprints:VIA_OSH4LAYER_MIN, F.Cu at (233.7, 63.5)
- added REF**: VIA_OSH4LAYER_MIN, vna_footprints:VIA_OSH4LAYER_MIN, F.Cu at (228.5, 68.5)
- added REF**: VIA_OSH4LAYER_MIN, vna_footprints:VIA_OSH4LAYER_MIN, F.Cu at (226.1, 68.3)
- added REF**: VIA_OSH4LAYER_MIN, vna_footprints:VIA_OSH4LAYER_MIN, F.Cu at (223.8, 68.3)
- added REF**: VIA_OSH4LAYER_MIN, vna_footprints:VIA_OSH4LAYER_MIN, F.Cu at (200.7, 63.5)
- added REF**: VIA_OSH4LAYER_MIN, vna_footprints:VIA_OSH4LAYER_MIN, F.Cu at (203.2, 58.4)
- added REF**: VIA_OSH4LAYER_MIN, vna_footprints:VIA_OSH4LAYER_MIN, F.Cu at (227.5, 42.5)
- added REF**: VIA_OSH4LAYER_MIN, vna_footprints:VIA_OSH4LAYER_MIN, F.Cu at (200.7, 58.4)
- added REF**: VIA_OSH4LAYER_MIN, vna_footprints:VIA_OSH4LAYER_MIN, F.Cu at (198.1, 58.4)
- added REF**: VIA_OSH4LAYER_MIN, vna_footprints:VIA_OSH4LAYER_MIN, F.Cu at (205.7, 50.8)
- added REF**: VIA_OSH4LAYER_MIN, vna_footprints:VIA_OSH4LAYER_MIN, F.Cu at (218.4, 45.7)
- added REF**: VIA_OSH4LAYER_MIN, vna_footprints:VIA_OSH4LAYER_MIN, F.Cu at (223.5, 40.6)
- added REF**: VIA_OSH4LAYER_MIN, vna_footprints:VIA_OSH4LAYER_MIN, F.Cu at (226.1, 35.6)
- added REF**: VIA_OSH4LAYER_MIN, vna_footprints:VIA_OSH4LAYER_MIN, F.Cu at (231.1, 35.6)
- added REF**: VIA_OSH4LAYER_MIN, vna_footprints:VIA_OSH4LAYER_MIN, F.Cu at (231.1, 38.1)
- added REF**: VIA_OSH4LAYER_MIN, vna_footprints:VIA_OSH4LAYER_MIN, F.Cu at (233.7, 40.6)
- added REF**: VIA_OSH4LAYER_MIN, vna_footprints:VIA_OSH4LAYER_MIN, F.Cu at (236.2, 40.6)
- moved U109 81.2 mm to (237.8, 44.8)
- moved C109 71.0 mm to (229.5, 41.7), turned to 270 degrees
- moved U104 70.5 mm to (212.4, 49.3)
- moved C115 70.0 mm to (204.1, 42.5), turned to 270 degrees
- moved R113 67.8 mm to (201.3, 45.7), turned to 180 degrees
- moved R112 66.2 mm to (199.3, 42.3), turned to 270 degrees
- moved C103 60.0 mm to (210.9, 53.2), turned to 270 degrees
- moved U107 59.8 mm to (229.7, 52.6), turned to 270 degrees
- moved C117 59.6 mm to (205.6, 42.8), turned to 270 degrees
- moved R107 59.1 mm to (212.2, 53.3), turned to 270 degrees
- moved C110 58.0 mm to (229.5, 48.5), turned to 90 degrees
- moved C104 57.9 mm to (213.2, 46.0)
- moved R110 56.0 mm to (229.5, 39.5), turned to 270 degrees
- moved H102 55.8 mm to (236.5, 36.8)
- moved R101 55.6 mm to (216.5, 61.5), turned to 180 degrees
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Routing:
- net +5V: track 0.00 -> 101.0 mm, vias 0 -> 5
- net GND: track 0.00 -> 86.5 mm, vias 0 -> 22
- net -5V: track 0.00 -> 71.3 mm, vias 0 -> 4
- net /PORT_SW: track 0.00 -> 54.4 mm, vias 0 -> 3
- net /V2: track 0.00 -> 43.2 mm, vias 0 -> 2
- net /V1: track 0.00 -> 37.2 mm, vias 0 -> 2
- net /-5V_EN: track 0.00 -> 29.2 mm, vias 0 -> 1
- net /MUL_EN: track 0.00 -> 22.3 mm
- net /MUL_SW: track 0.00 -> 21.9 mm, vias 0 -> 1
- net Net-(C116-Pad1): track 0.00 -> 14.5 mm
- net Net-(U102-Pad11): track 0.00 -> 12.1 mm
- net Net-(U104-Pad4): track 0.00 -> 9.19 mm
- net Net-(C106-Pad2): track 0.00 -> 8.22 mm
- net Net-(C113-Pad2): track 0.00 -> 5.93 mm
- net Net-(C114-Pad2): track 0.00 -> 5.17 mm
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- added copper zone on F.Cu, net GND
- added copper zone on In2.Cu, net GND
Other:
- board outline added: 43.2 x 35.6 mm
- copper layers 2 -> 4
- net class Default: clearance 0.2 -> 0.1524
- rule trace_clearance: 0.2 -> 0.1524
- rule trace_min: 0.2 -> 0.1524
- board text added: "0v -en pw mw me 5v"
- board text added: "2017.06"
- board text added: "PORT 1"
- board text added: "PORT 2"
- board text added: "RF IN"
- board text added: "VNA PORT SWITCH r0"
